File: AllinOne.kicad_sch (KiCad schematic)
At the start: 268 parts, among them SW0 SW_Push, SW1 SW_Push, SW10 SW_Push, SW100 SW_Push, SW101 SW_Push, SW102 SW_Push, SW103 SW_Push, SW104 SW_Push, SW105 SW_Push, SW106 SW_Push, SW107 SW_Push, SW108 SW_Push, SW109 SW_Push, SW11 SW_Push, SW110 SW_Push, SW111 SW_Push, SW114 SW_Push, SW116 SW_Push, SW117 SW_Push, SW118 SW_Push, SW119 SW_Push, SW12 SW_Push, SW120 SW_Push, SW121 SW_Push, SW122 SW_Push, SW126 SW_Push, SW13 SW_Push, SW130 SW_Push, SW131 SW_Push, SW132 SW_Push, SW133 SW_Push, SW134 SW_Push, SW135 SW_Push, SW136 SW_Push, SW137 SW_Push, SW138 SW_Push, SW139 SW_Push, SW14 SW_Push, SW15 SW_Push, SW16 SW_Push, SW18 SW_Push, SW19 SW_Push, SW2 SW_Push, SW20 SW_Push, SW21 SW_Push, SW22 SW_Push, SW23 SW_Push, SW24 SW_Push, SW25 SW_Push, SW26 SW_Push, SW27 SW_Push, SW28 SW_Push, SW29 SW_Push, SW3 SW_Push, SW30 SW_Push, SW31 SW_Push, SW32 SW_Push, SW33 SW_Push, SW34 SW_Push, SW35 SW_Push, SW36 SW_Push, SW37 SW_Push, SW38 SW_Push, SW39 SW_Push, SW4 SW_Push, SW40 SW_Push, SW41 SW_Push, SW42 SW_Push, SW43 SW_Push, SW44 SW_Push, SW45 SW_Push, SW46 SW_Push, SW47 SW_Push, SW48 SW_Push, SW49 SW_Push, SW5 SW_Push, SW50 SW_Push, SW51 SW_Push, SW52 SW_Push, SW53 SW_Push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

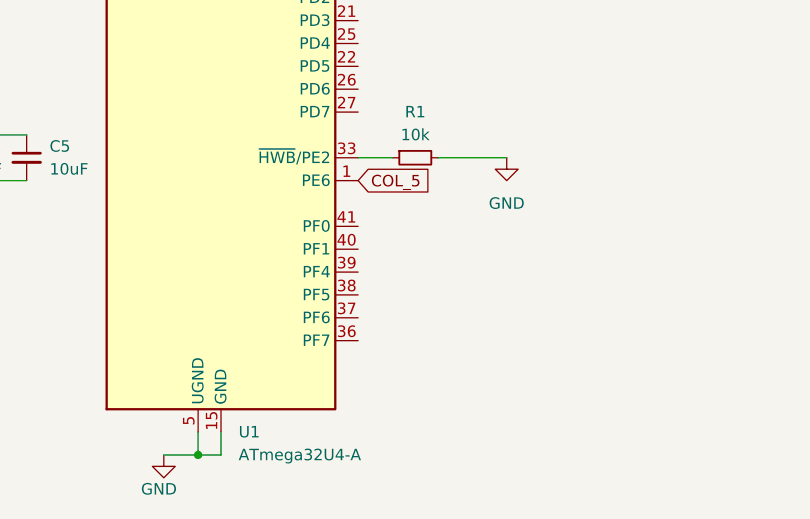
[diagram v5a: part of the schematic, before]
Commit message: Almost done wiring to the mcu
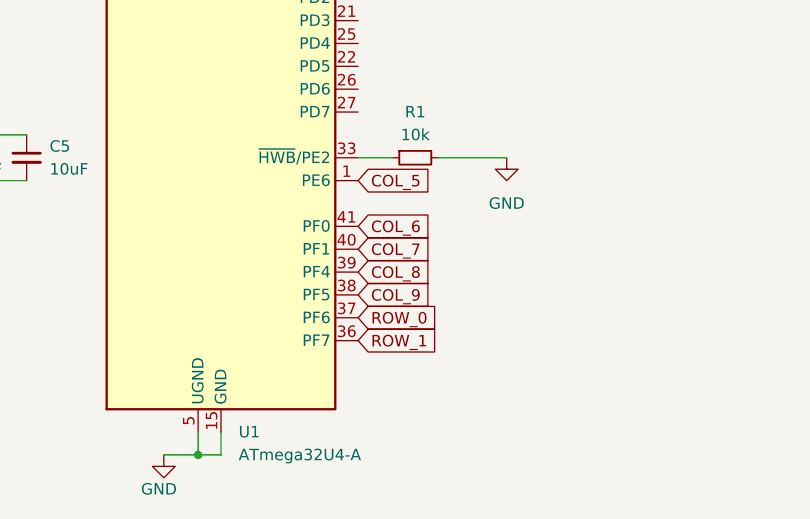
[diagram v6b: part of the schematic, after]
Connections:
- net COL_6: now also U1.41 (PF0)
- net COL_7: now also U1.40 (PF1)
- net COL_8: now also U1.39 (PF4)
- net COL_9: now also U1.38 (PF5)
- net ROW_0: now also U1.37 (PF6)
- net ROW_1: now also U1.36 (PF7)
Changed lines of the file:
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@@
+    )
+  )
+  (global_label "ROW_1" (shape input) (at 87.63 252.73 0) (fields_autoplaced)
+    (effects (font (size 1.27 1.27)) (justify left))
+    (property "Intersheetrefs" "${INTERSHEET_REFS}" (at 96.7648 252.73 0)
+      (effects (font (size 1.27 1.27)) (justify left) hide)
     )
   )
@@
     )
   )
+  (global_label "COL_8" (shape input) (at 87.63 245.11 0) (fields_autoplaced)
+    (effects (font (size 1.27 1.27)) (justify left))
+    (property "Intersheetrefs" "${INTERSHEET_REFS}" (at 96.3415 245.11 0)
+      (effects (font (size 1.27 1.27)) (justify left) hide)
+    )
+  )
+  (global_label "COL_7" (shape input) (at 87.63 242.57 0) (fields_autoplaced)
+    (effects (font (size 1.27 1.27)) (justify left))
+    (property "Intersheetrefs" "${INTERSHEET_REFS}" (at 96.3415 242.57 0)
+      (effects (font (size 1.27 1.27)) (justify left) hide)
+    )
+  )
   (global_label "COL_4" (shape input) (at 218.44 27.94 90) (fields_autoplaced)
     (effects (font (size 1.27 1.27)) (justify left))
     (property "Intersheetrefs" "${INTERSHEET_REFS}" (at 218.44 19.2285 90)
+      (effects (font (size 1.27 1.27)) (justify left) hide)
+    )
+  )
+  (global_label "ROW_0" (shape input) (at 87.63 250.19 0) (fields_autoplaced)
+    (effects (font (size 1.27 1.27)) (justify left))
+    (property "Intersheetrefs" "${INTERSHEET_REFS}" (at 96.7648 250.19 0)
       (effects (font (size 1.27 1.27)) (justify left) hide)
     )
@@
     )
   )
+  (global_label "COL_9" (shape input) (at 87.63 247.65 0) (fields_autoplaced)
+    (effects (font (size 1.27 1.27)) (justify left))
+    (property "Intersheetrefs" "${INTERSHEET_REFS}" (at 96.3415 247.65 0)
+      (effects (font (size 1.27 1.27)) (justify left) hide)
+    )
+  )
   (global_label "COL_2" (shape input) (at 87.63 184.15 0) (fields_autoplaced)
     (effects (font (size 1.27 1.27)) (justify left))
@@
       (effects (font (size 1.27 1.27)) (justify left) hide)
     )
+  )
+  (global_label "COL_6" (shape input) (at 87.63 240.03 0) (fields_autoplaced)
+    (effects (font (size 1.27 1.27)) (justify left))
+    (property "Intersheetrefs" "${INTERSHEET_REFS}" (at 96.3415 240.03 0)
+      (effects (font (size 1.27 1.27)) (justify left) hide)
+    )

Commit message: All Done for now
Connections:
- net ROW_10: now also U1.22 (PD5)
- net ROW_11: now also U1.21 (PD3)
- net ROW_12: now also U1.20 (PD2)
- net ROW_13: now also U1.19 (PD1)
- net ROW_2: now also U1.32 (PC7)
- net ROW_3: now also U1.31 (PC6)
- net ROW_4: now also U1.30 (PB6)
- net ROW_5: now also U1.29 (PB5)
- net ROW_6: now also U1.28 (PB4)
- net ROW_7: now also U1.27 (PD7)
- net ROW_8: now also U1.26 (PD6)
- net ROW_9: now also U1.25 (PD4)
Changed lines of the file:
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@@
     (stroke (width 0) (type default))
   )
+  (global_label "ROW_5" (shape input) (at 87.63 191.77 0) (fields_autoplaced)
+    (effects (font (size 1.27 1.27)) (justify left))
+    (property "Intersheetrefs" "${INTERSHEET_REFS}" (at 96.7648 191.77 0)
+      (effects (font (size 1.27 1.27)) (justify left) hide)
+    )
+  )
   (global_label "COL_6" (shape input) (at 289.56 27.94 90) (fields_autoplaced)
     (effects (font (size 1.27 1.27)) (justify left))
@@
     )
   )
+  (global_label "ROW_6" (shape input) (at 87.63 189.23 0) (fields_autoplaced)
+    (effects (font (size 1.27 1.27)) (justify left))
+    (property "Intersheetrefs" "${INTERSHEET_REFS}" (at 96.7648 189.23 0)
+      (effects (font (size 1.27 1.27)) (justify left) hide)
+    )
+  )
+  (global_label "ROW_10" (shape input) (at 87.63 222.25 0) (fields_autoplaced)
+    (effects (font (size 1.27 1.27)) (justify left))
+    (property "Intersheetrefs" "${INTERSHEET_REFS}" (at 97.9743 222.25 0)
+      (effects (font (size 1.27 1.27)) (justify left) hide)
+    )
+  )
   (global_label "ROW_7" (shape input) (at 30.48 109.22 180) (fields_autoplaced)
     (effects (font (size 1.27 1.27)) (justify right))
@@
     )
   )
+  (global_label "ROW_2" (shape input) (at 87.63 204.47 0) (fields_autoplaced)
+    (effects (font (size 1.27 1.27)) (justify left))
+    (property "Intersheetrefs" "${INTERSHEET_REFS}" (at 96.7648 204.47 0)
+      (effects (font (size 1.27 1.27)) (justify left) hide)
+    )
+  )
   (global_label "COL_0" (shape input) (at 76.2 27.94 90) (fields_autoplaced)
     (effects (font (size 1.27 1.27)) (justify left))
@@
     )
   )
+  (global_label "ROW_7" (shape input) (at 87.63 227.33 0) (fields_autoplaced)
+    (effects (font (size 1.27 1.27)) (justify left))
+    (property "Intersheetrefs" "${INTERSHEET_REFS}" (at 96.7648 227.33 0)
+      (effects (font (size 1.27 1.27)) (justify left) hide)
+    )
+  )
   (global_label "COL_7" (shape input) (at 87.63 242.57 0) (fields_autoplaced)
     (effects (font (size 1.27 1.27)) (justify left))
@@
     )
   )
+  (global_label "ROW_8" (shape input) (at 87.63 224.79 0) (fields_autoplaced)
+    (effects (font (size 1.27 1.27)) (justify left))
+    (property "Intersheetrefs" "${INTERSHEET_REFS}" (at 96.7648 224.79 0)
+      (effects (font (size 1.27 1.27)) (justify left) hide)
+    )
+  )
   (global_label "ROW_0" (shape input) (at 87.63 250.19 0) (fields_autoplaced)
     (effects (font (size 1.27 1.27)) (justify left))
@@
     )
   )
+  (global_label "ROW_12" (shape input) (at 87.63 214.63 0) (fields_autoplaced)
+    (effects (font (size 1.27 1.27)) (justify left))
+    (property "Intersheetrefs" "${INTERSHEET_REFS}" (at 97.9743 214.63 0)
+      (effects (font (size 1.27 1.27)) (justify left) hide)
+    )
+  )
   (global_label "COL_3" (shape input) (at 182.88 27.94 90) (fields_autoplaced)
     (effects (font (size 1.27 1.27)) (justify left))
@@
     )
   )
+  (global_label "ROW_3" (shape input) (at 87.63 201.93 0) (fields_autoplaced)
+    (effects (font (size 1.27 1.27)) (justify left))
+    (property "Intersheetrefs" "${INTERSHEET_REFS}" (at 96.7648 201.93 0)
+      (effects (font (size 1.27 1.27)) (justify left) hide)
+    )
+  )
+  (global_label "ROW_11" (shape input) (at 87.63 217.17 0) (fields_autoplaced)
+    (effects (font (size 1.27 1.27)) (justify left))
+    (property "Intersheetrefs" "${INTERSHEET_REFS}" (at 97.9743 217.17 0)
+      (effects (font (size 1.27 1.27)) (justify left) hide)
+    )
+  )
   (global_label "ROW_11" (shape input) (at 30.48 139.7 180) (fields_autoplaced)
     (effects (font (size 1.27 1.27)) (justify right))
@@
     )
   )
+  (global_label "ROW_9" (shape input) (at 87.63 219.71 0) (fields_autoplaced)
+    (effects (font (size 1.27 1.27)) (justify left))
+    (property "Intersheetrefs" "${INTERSHEET_REFS}" (at 96.7648 219.71 0)
+      (effects (font (size 1.27 1.27)) (justify left) hide)
+    )
+  )
+  (global_label "ROW_13" (shape input) (at 87.63 212.09 0) (fields_autoplaced)
+    (effects (font (size 1.27 1.27)) (justify left))
+    (property "Intersheetrefs" "${INTERSHEET_REFS}" (at 97.9743 212.09 0)
+      (effects (font (size 1.27 1.27)) (justify left) hide)
+    )
+  )
   (global_label "COL_5" (shape input) (at 254 27.94 90) (fields_autoplaced)
     (effects (font (size 1.27 1.27)) (justify left))
@@
       (effects (font (size 1.27 1.27)) (justify left) hide)
     )
+  )
+  (global_label "ROW_4" (shape input) (at 87.63 194.31 0) (fields_autoplaced)
+    (effects (font (size 1.27 1.27)) (justify left))
+    (property "Intersheetrefs" "${INTERSHEET_REFS}" (at 96.7648 194.31 0)
+      (effects (font (size 1.27 1.27)) (justify left) hide)
+    )
